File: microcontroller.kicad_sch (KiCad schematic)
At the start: 16 parts, among them SW1 System Reset, SW2 Boot Switch, U1 STM32F446RETx

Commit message: remove redundant stm32f44 document folder. remove USB pinouts and references
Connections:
- net USB_DN: no longer names the net of U1.44 (PA11)
- net USB_DP: no longer names the net of U1.45 (PA12)
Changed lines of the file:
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@@
 	(text "Power Supply Scheme"
 		(exclude_from_sim no)
-		(at 70.866 19.304 0)
+		(at 54.864 19.558 0)
 		(effects
 			(font
@@
 	(wire
 		(pts
-			(xy 146.05 102.87) (xy 175.26 102.87)
-		)
-		(stroke
-			(width 0)
-			(type default)
-		)
-	)
-	(wire
-		(pts
 			(xy 166.37 130.81) (xy 146.05 130.81)
 		)
@@
 		(pts
 			(xy 146.05 135.89) (xy 176.53 135.89)
-		)
-		(stroke
-			(width 0)
-			(type default)
-		)
-	)
-	(wire
-		(pts
-			(xy 146.05 100.33) (xy 175.26 100.33)
 		)
 		(stroke
@@
 		)
 	)
-	(hierarchical_label "USB_DN"
-		(shape bidirectional)
-		(at 175.26 100.33 0)
-		(effects
-			(font
-				(size 1.27 1.27)
-			)
-			(justify left)
-		)
-	)
 	(hierarchical_label "BUZZ"
 		(shape output)
@@
 		(effects
 			(font
-				(size 1.27 1.27)
-			)
-			(justify left)
-		)
-	)
-	(hierarchical_label "USB_DP"
-		(shape bidirectional)
-		(at 175.26 102.87 0)
-		(effects
-			(font

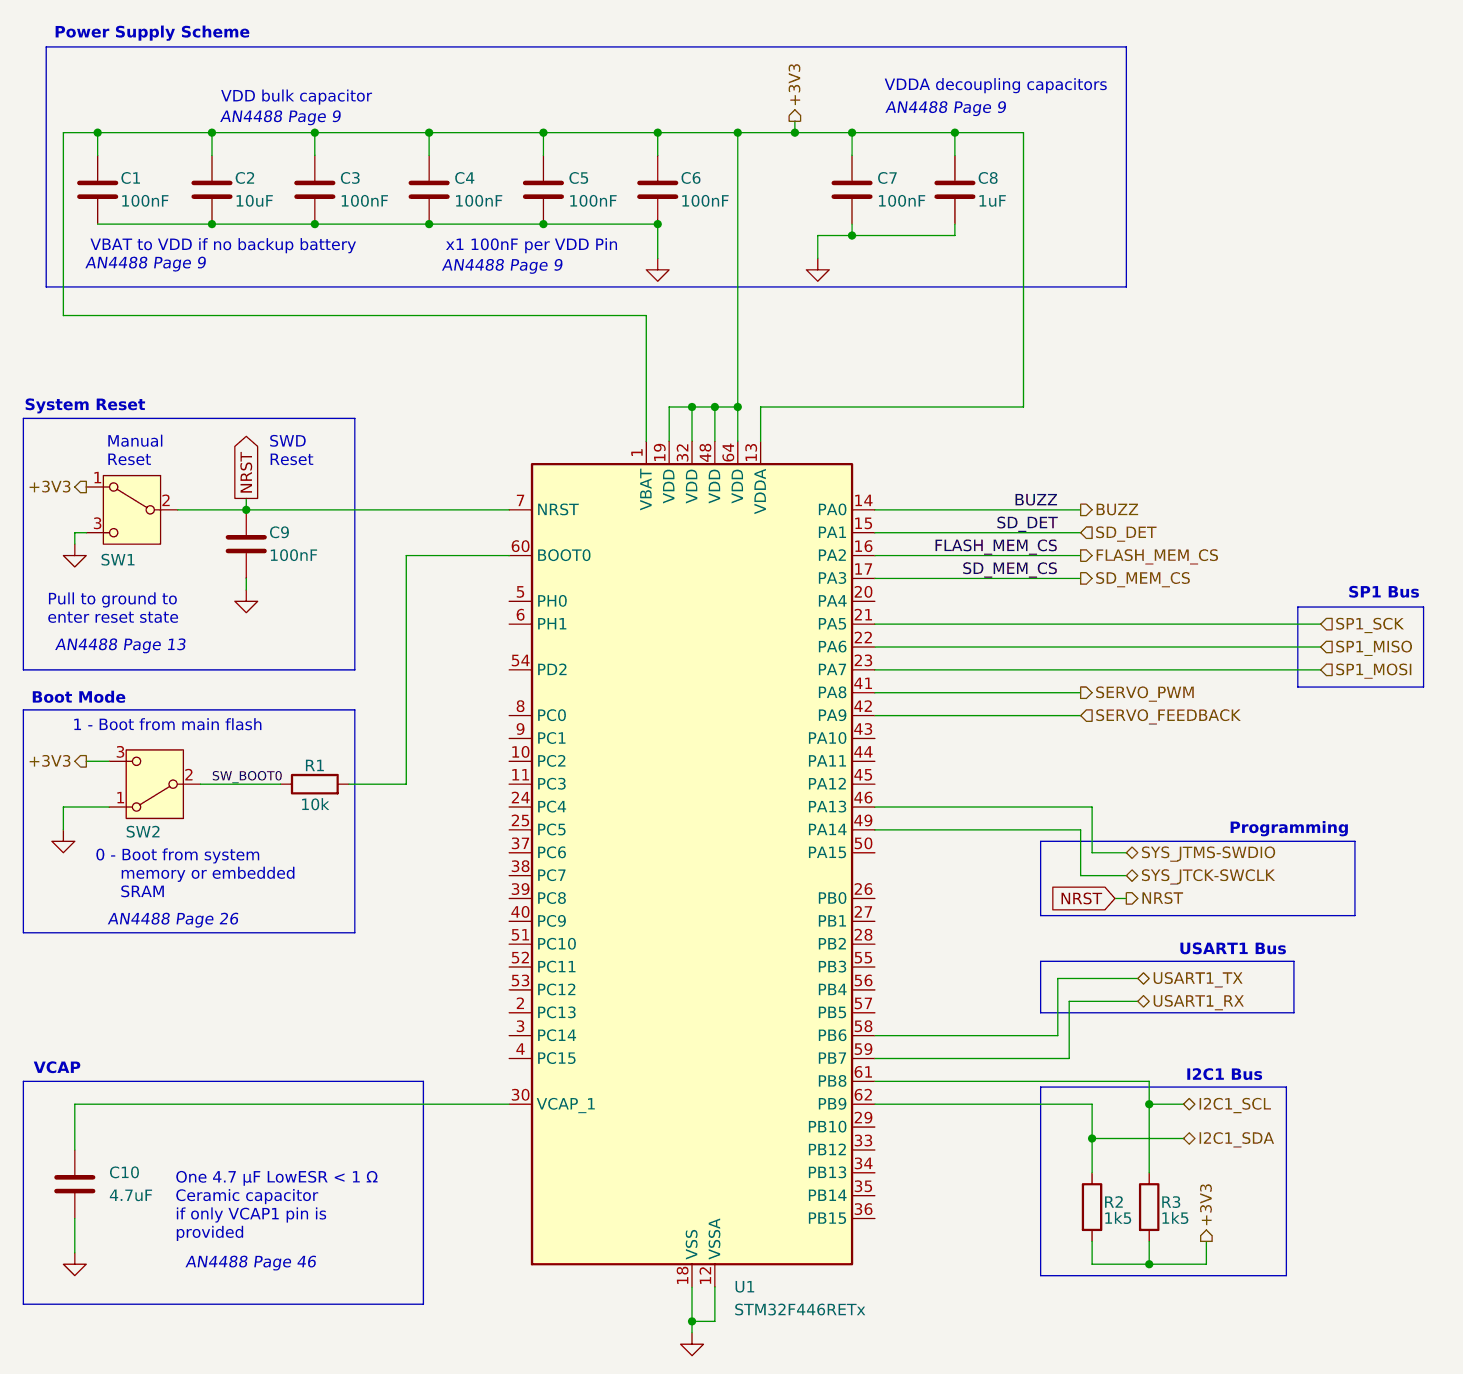
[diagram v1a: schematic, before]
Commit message: fix spi labels. add non connect markers
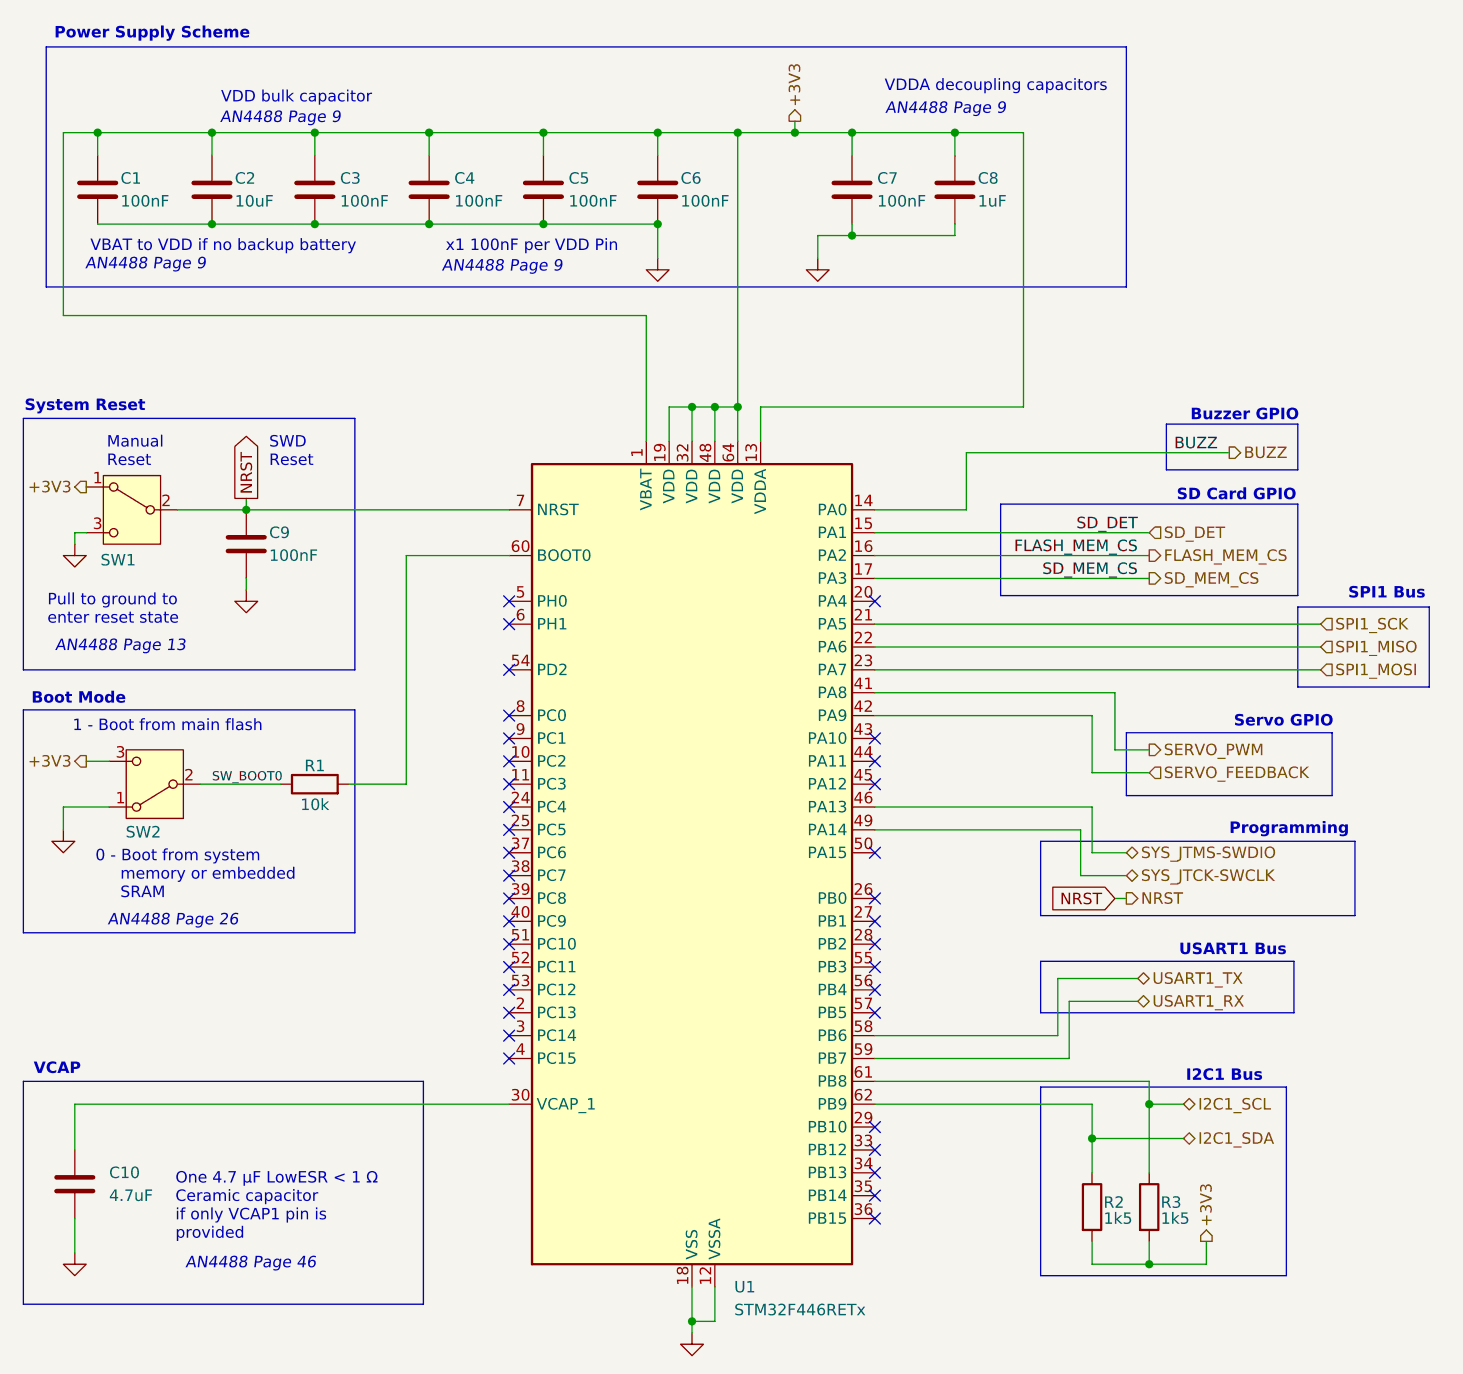
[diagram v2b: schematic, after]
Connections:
- net SP1_MISO renamed SPI1_MISO
- net SP1_MOSI renamed SPI1_MOSI
- net SP1_SCK renamed SPI1_SCK
- no-connect marks 0 -> 35
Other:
- note added: "Buzzer GPIO"
- note added: "SD Card GPIO"
- note added: "SPI1 Bus"
- note added: "Servo GPIO"
- note removed: "SP1 Bus"
